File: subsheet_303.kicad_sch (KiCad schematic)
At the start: 4 parts, among them U303 8.010613 MHz, U304 74LS74_PHY

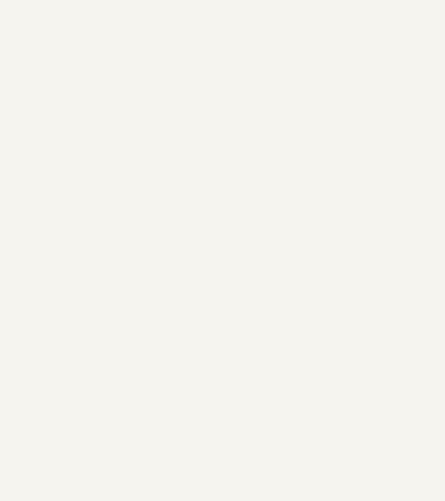
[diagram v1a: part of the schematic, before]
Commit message: add gnd/vcc symbol to start replacing local labels
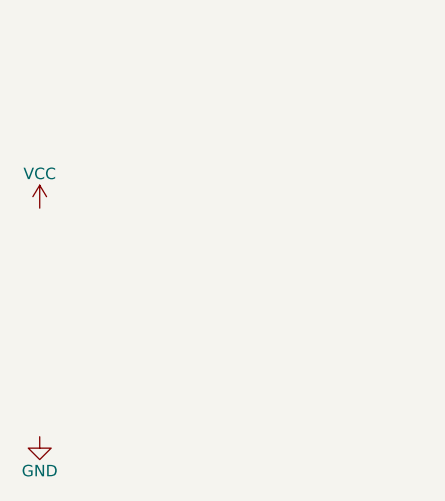
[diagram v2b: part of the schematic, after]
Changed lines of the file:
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@@
     (pin "8")
   )
+  (symbol (lib_id "power:GND") (at 22.86 246.38 0) (unit 1)
+    (in_bom yes) (on_board yes)
+    (property "Reference" "#PWR?" (id 0) (at 22.86 252.73 0)
+      (effects (font (size 1.27 1.27)) hide)
+    )
+    (property "Value" "GND" (id 1) (at 22.86 250.19 0))
+    (property "Footprint" "" (id 2) (at 22.86 246.38 0)
+      (effects (font (size 1.27 1.27)) hide)
+    )
+    (property "Datasheet" "" (id 3) (at 22.86 246.38 0)
+      (effects (font (size 1.27 1.27)) hide)
+    )
+    (pin "1")
+  )
+  (symbol (lib_id "power:VCC") (at 22.86 220.98 0) (unit 1)
+    (in_bom yes) (on_board yes)
+    (property "Reference" "#PWR?" (id 0) (at 22.86 224.79 0)
+      (effects (font (size 1.27 1.27)) hide)
+    )
+    (property "Value" "VCC" (id 1) (at 22.86 217.17 0))
+    (property "Footprint" "" (id 2) (at 22.86 220.98 0)
+      (effects (font (size 1.27 1.27)) hide)
+    )
+    (property "Datasheet" "" (id 3) (at 22.86 220.98 0)
+      (effects (font (size 1.27 1.27)) hide)
+    )
+    (pin "1")
+  )
 )
